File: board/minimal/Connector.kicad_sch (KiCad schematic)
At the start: 7 parts, among them J12 Debug, J13 9DoF, J14 Temperature, J15 UltraSonic, J16 OLED

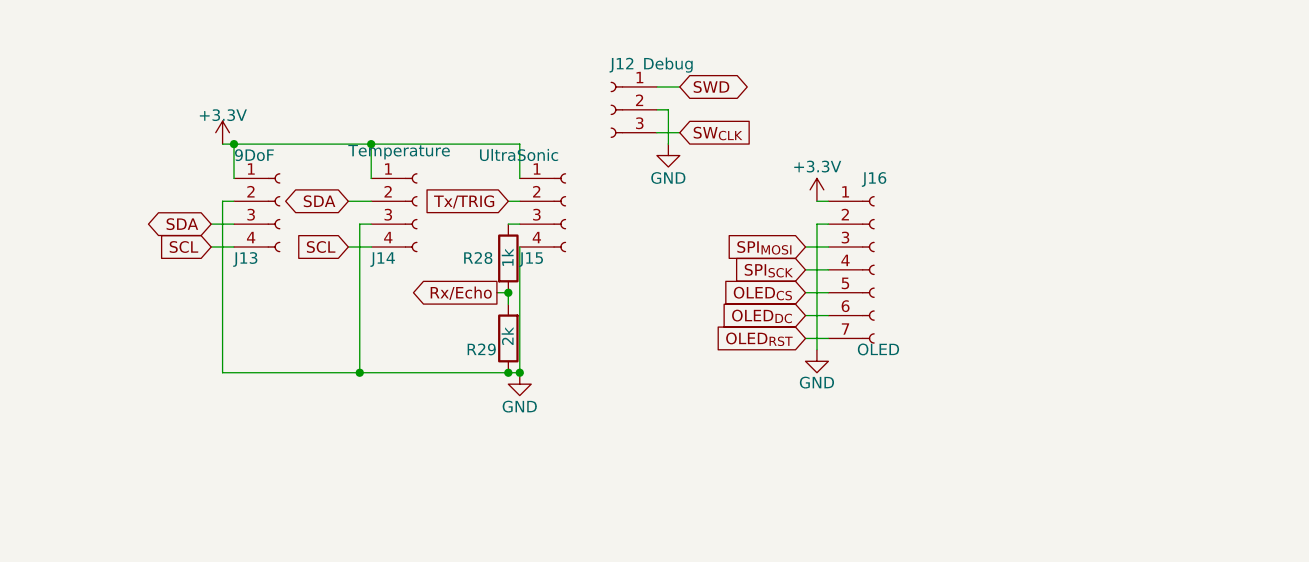
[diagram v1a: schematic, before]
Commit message: add some connectors
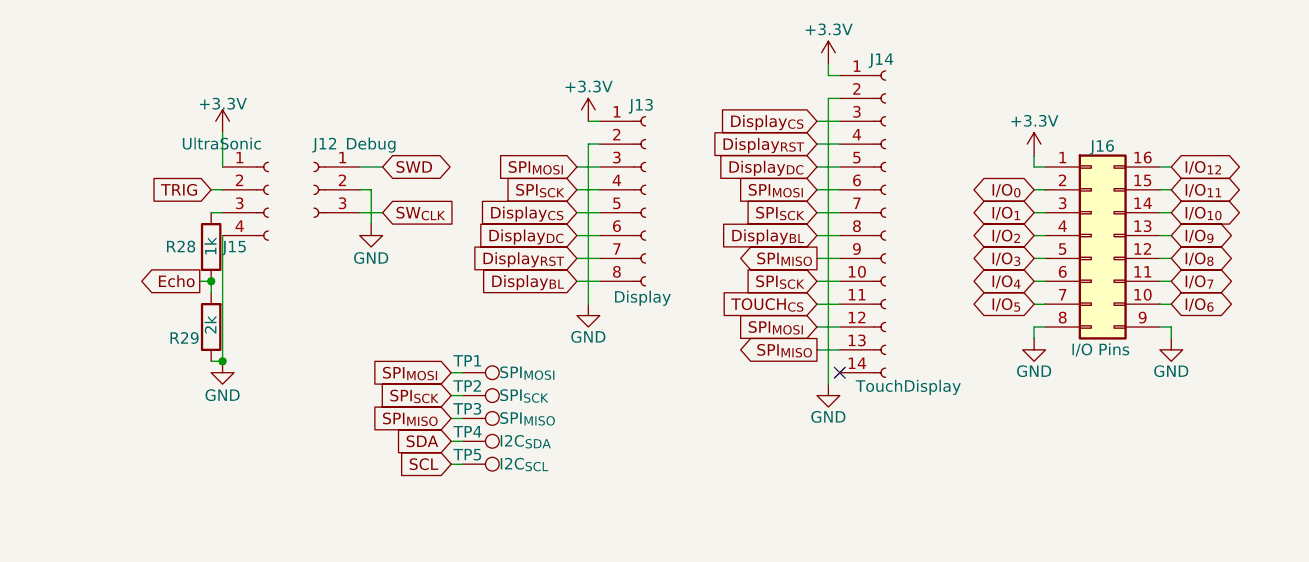
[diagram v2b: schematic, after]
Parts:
- removed J13: 9DoF, Connector_JST:JST_XH_S4B-XH-A_1x04_P2.50mm_Horizontal, symbol Connector:Conn_01x04_Socket
- removed J14: Temperature, Connector_PinSocket_2.54mm:PinSocket_1x04_P2.54mm_Vertical, symbol Connector:Conn_01x04_Socket
- removed J16: OLED, Connector_JST:JST_XH_S7B-XH-A_1x07_P2.50mm_Horizontal, symbol Connector:Conn_01x07_Socket
- added J13: Display, symbol Connector:Conn_01x08_Socket
- added J14: TouchDisplay, symbol Connector:Conn_01x14_Socket
- added J16: I/O Pins, symbol Connector_Generic:Conn_02x08_Counter_Clockwise
- added TP1: SPI_{MOSI}, symbol Connector:TestPoint
- added TP2: SPI_{SCK}, symbol Connector:TestPoint
- added TP3: SPI_{MISO}, symbol Connector:TestPoint
- added TP4: I2C_{SDA}, symbol Connector:TestPoint
- added TP5: I2C_{SCL}, symbol Connector:TestPoint
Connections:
- net +3.3V: now also J13.1 (Pin_1), J14.1 (Pin_1), J16.1 (Pin_1)
- net GND: now also J13.2 (Pin_2), J14.2 (Pin_2), J16.8 (Pin_8), J16.9 (Pin_9)
- net SCL: now also TP5.1
- net SDA: now also TP4.1
- net SPI_{MOSI}: now also J13.3 (Pin_3), J14.12 (Pin_12), J14.6 (Pin_6), TP1.1
- net SPI_{SCK}: now also J13.4 (Pin_4), J14.10 (Pin_10), J14.7 (Pin_7), TP2.1
- net Rx/Echo renamed Echo
- net Tx/TRIG renamed TRIG
- new net Display_{BL}: J13.8 (Pin_8), J14.8 (Pin_8)
- new net Display_{CS}: J13.5 (Pin_5), J14.3 (Pin_3)
- new net Display_{DC}: J13.6 (Pin_6), J14.5 (Pin_5)
- new net Display_{RST}: J13.7 (Pin_7), J14.4 (Pin_4)
- new net I/O_{0}: J16.2 (Pin_2)
- new net I/O_{10}: J16.14 (Pin_14)
- new net I/O_{11}: J16.15 (Pin_15)
- new net I/O_{12}: J16.16 (Pin_16)
- new net I/O_{1}: J16.3 (Pin_3)
- new net I/O_{2}: J16.4 (Pin_4)
- new net I/O_{3}: J16.5 (Pin_5)
- new net I/O_{4}: J16.6 (Pin_6)
- new net I/O_{5}: J16.7 (Pin_7)
- new net I/O_{6}: J16.10 (Pin_10)
- new net I/O_{7}: J16.11 (Pin_11)
- new net I/O_{8}: J16.12 (Pin_12)
- new net I/O_{9}: J16.13 (Pin_13)
- new net SPI_{MISO}: J14.13 (Pin_13), J14.9 (Pin_9), TP3.1
- new net TOUCH_{CS}: J14.11 (Pin_11)
- no-connect marks 0 -> 1
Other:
- moved on the sheet: J12, J15, R28, R29

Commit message: set footprint
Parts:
- J15: renamed from J13; footprint (none) -> Connector_PinHeader_2.54mm:PinHeader_1x08_P2.54mm_Horizontal
- J16: renamed from J14; footprint (none) -> Connector_PinSocket_2.54mm:PinSocket_1x14_P2.54mm_Vertical
- J17: renamed from J16; footprint (none) -> Connector_PinSocket_2.54mm:PinSocket_2x08_P2.54mm_Vertical
- TP2: renamed from TP1; footprint (none) -> TestPoint:TestPoint_Loop_D2.50mm_Drill1.85mm
- TP3: renamed from TP2; footprint (none) -> TestPoint:TestPoint_Loop_D2.50mm_Drill1.85mm
- TP4: renamed from TP3; footprint (none) -> TestPoint:TestPoint_Loop_D2.50mm_Drill1.85mm
- TP5: renamed from TP4; footprint (none) -> TestPoint:TestPoint_Loop_D2.50mm_Drill1.85mm
- TP6: renamed from TP5; footprint (none) -> TestPoint:TestPoint_Loop_D2.50mm_Drill1.85mm
- renumbered J15 to J13, J12 to J14, R28 to R30
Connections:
- net Echo: now also R30.1; no longer R30.2
- net at J13.3 (Pin_3): now also R30.2; no longer R30.1
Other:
- moved on the sheet: R29, R30

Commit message: add testpoint for gnd and pic of schematics
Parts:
- added TP7: GND, TestPoint:TestPoint_Loop_D2.50mm_Drill1.85mm, symbol Connector:TestPoint
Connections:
- net GND: now also TP7.1
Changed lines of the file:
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@@
+	(wire
+		(pts
+			(xy 153.67 130.81) (xy 153.67 132.08)
+		)
+		(stroke
+			(width 0)
+			(type default)
+		)
+	)
 	(wire
 		(pts
@@
 				(path "/7af2d99d-e350-48e7-86b4-20911ea922f3/42224473-68eb-43d4-97ed-5df85a0a50dc"
 					(reference "R30")
+					(unit 1)
+				)
+			)
+		)
+	)
+	(symbol
+		(lib_id "power:GND")
+		(at 153.67 132.08 0)
+		(unit 1)
+		(exclude_from_sim no)
+		(in_bom yes)
+		(on_board yes)
+		(dnp no)
+		(property "Reference" "#PWR080"
+			(at 153.67 138.43 0)
+			(hide yes)
+			(effects
+				(font
+					(size 1.27 1.27)
+				)
+			)
+		)
+		(property "Value" "GND"
+			(at 153.67 135.763 0)
+			(effects
+				(font
+					(size 1.27 1.27)
+				)
+			)
+		)
+		(property "Footprint" ""
+			(at 153.67 132.08 0)
+			(hide yes)
+			(effects
+				(font
+					(size 1.27 1.27)
+				)
+			)
+		)
+		(property "Datasheet" ""
+			(at 153.67 132.08 0)
+			(hide yes)
+			(effects
+				(font
+					(size 1.27 1.27)
+				)
+			)
+		)
+		(property "Description" ""
+			(at 153.67 132.08 0)
+			(effects
+				(font
+					(size 1.27 1.27)
+				)
+			)
+		)
+		(pin "1"
+		)
+		(instances
+			(project "TurtlePico-Minimal"
+				(path "/7af2d99d-e350-48e7-86b4-20911ea922f3/42224473-68eb-43d4-97ed-5df85a0a50dc"
+					(reference "#PWR080")
 					(unit 1)
 				)
@@
 					(unit 1)
 				)
+			)
+		)
+	)
+	(symbol
+		(lib_id "Connector:TestPoint")
+		(at 153.67 130.81 270)
+		(unit 1)
+		(exclude_from_sim no)
+		(in_bom yes)
+		(on_board yes)
+		(dnp no)
+		(property "Reference" "TP7"
+			(at 152.654 129.794 90)
+			(effects
+				(font
+					(size 1.27 1.27)
+				)
+				(justify left)
+			)
+		)
+		(property "Value" "GND"
+			(at 157.734 130.81 90)
+			(effects
+				(font
+					(size 1.27 1.27)
+				)
+				(justify left)
+			)
+		)
+		(property "Footprint" "TestPoint:TestPoint_Loop_D2.50mm_Drill1.85mm"
+			(at 153.67 135.89 0)
+			(hide yes)
+			(effects
+				(font
+					(size 1.27 1.27)
+				)
+			)
+		)
+		(property "Datasheet" ""
+			(at 153.67 135.89 0)
+			(hide yes)
+			(effects
+				(font
+					(size 1.27 1.27)
+				)
+			)
+		)
+		(property "Description" "test point"
+			(at 153.67 130.81 0)
+			(hide yes)
+			(effects
+				(font
+					(size 1.27 1.27)
+				)
+			)
+		)
+		(pin "1"
+		)
+		(instances
+			(project "TurtlePico-Minimal"
+				(path "/7af2d99d-e350-48e7-86b4-20911ea922f3/42224473-68eb-43d4-97ed-5df85a0a50dc"
+					(reference "TP7")
+					(unit 1)
+				)
